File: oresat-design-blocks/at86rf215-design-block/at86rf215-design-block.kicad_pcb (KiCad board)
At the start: 4 copper layers, 61.3 x 44.1 mm, 76 parts, among them J1 SMA, J10 Conn_01x08, J11 Conn_01x05, J12 Conn_01x08, J2 USB4105-GF-A, J3 Conn_01x06, J4 SMA, J6 Conn_01x06, J7 SMA, J8 SMA, J9 Screw_Terminal_01x02, SW1 RESET, U1 AT86RF215, U2 LP2985AIM5-1.8_NOPB, U3 2450FB15A050E, U5 QPC1022, U7 NCS2-62+, X1 TXETALSANF-26.000000

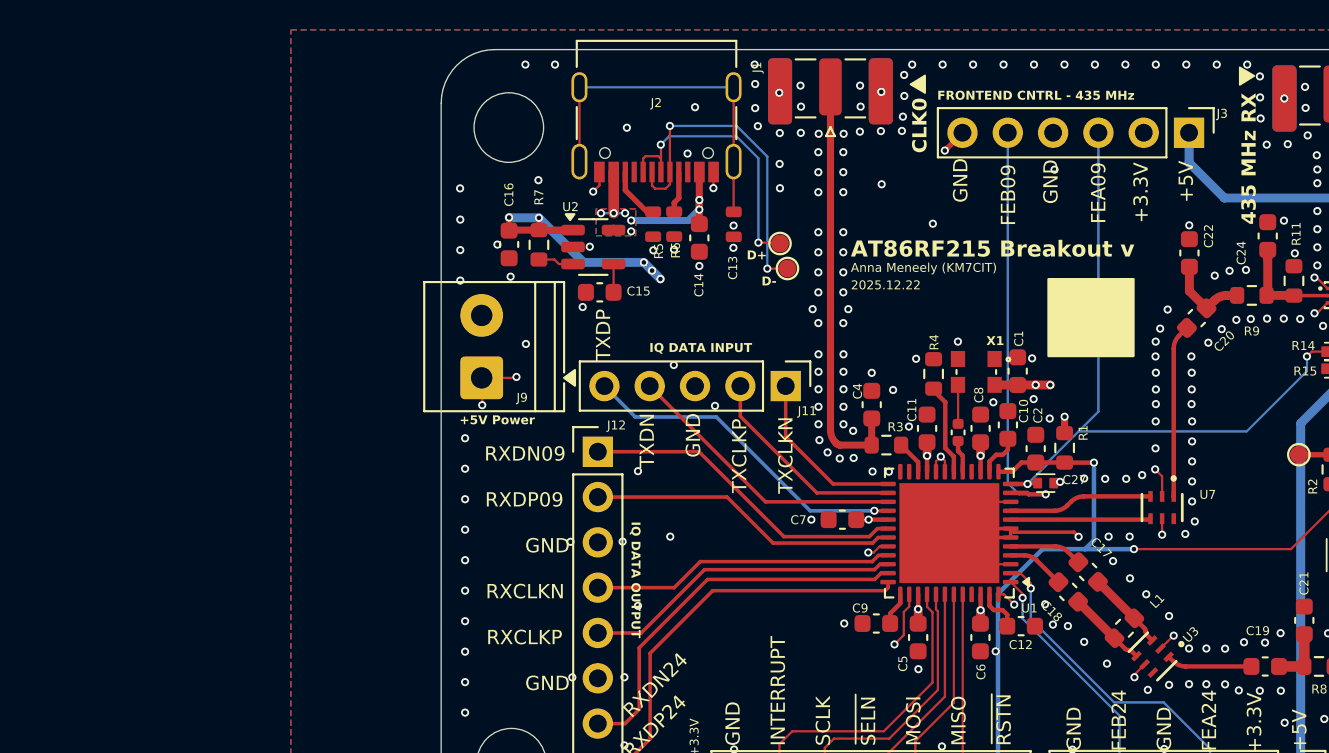
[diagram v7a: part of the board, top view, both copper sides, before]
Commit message: Design review on AT86 breakout.
Added LEDs (you're welcome Theo), changed resistor values to be more matchy, deleted some unecessary grounds in layout, switching to 0603 and BOM still left.
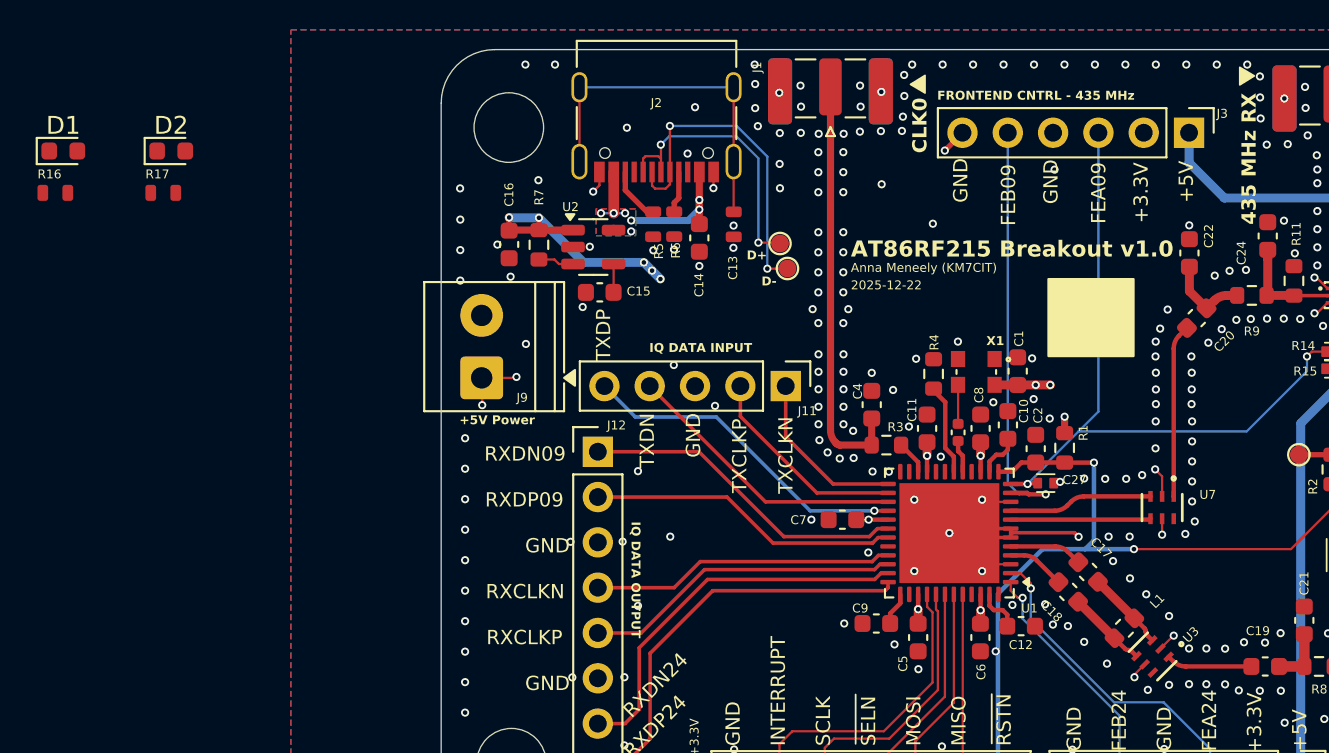
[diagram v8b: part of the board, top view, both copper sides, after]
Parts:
- added D1: GRN, LED_SMD:LED_0603_1608Metric, F.Cu at (69.6, 60.0)
- added D2: AMB, LED_SMD:LED_0603_1608Metric, F.Cu at (75.7, 60.0)
- added R16: 5.1k, oresat-passives:0603-C-NOSILK, F.Cu at (69.2, 62.4)
- added R17: 5.1k, oresat-passives:0603-C-NOSILK, F.Cu at (75.2, 62.4)
- R13: value 5.62k -> 5.1k
- R14: value 3k -> 5.1k
- R15: value 5k -> 10k
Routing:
- net GND: track 42.2 -> 35.1 mm, vias 354 -> 359
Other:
- board text removed: "2025.12.22"
